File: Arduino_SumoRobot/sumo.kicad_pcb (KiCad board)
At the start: 2 copper layers, 66 x 53.3 mm, 45 parts, among them IC1 40106D, J1 HEADER_4, K1 RELAY_C, K2 RELAY_C, K3 RELAY_C, K4 RELAY_C, P1 Power, P10 CONN_01X04, P11 CONN_01X04, P12 CONN_01X02, P2 Analog, P3 Digital, P4 Digital, P5 CONN_1, P7 CONN_1, P9 CONN_01X06, Q1 S8050, Q2 S8050, Q3 S8050, Q4 S8050, U1 CNY70, U2 CNY70, U3 CNY70, U4 CNY70

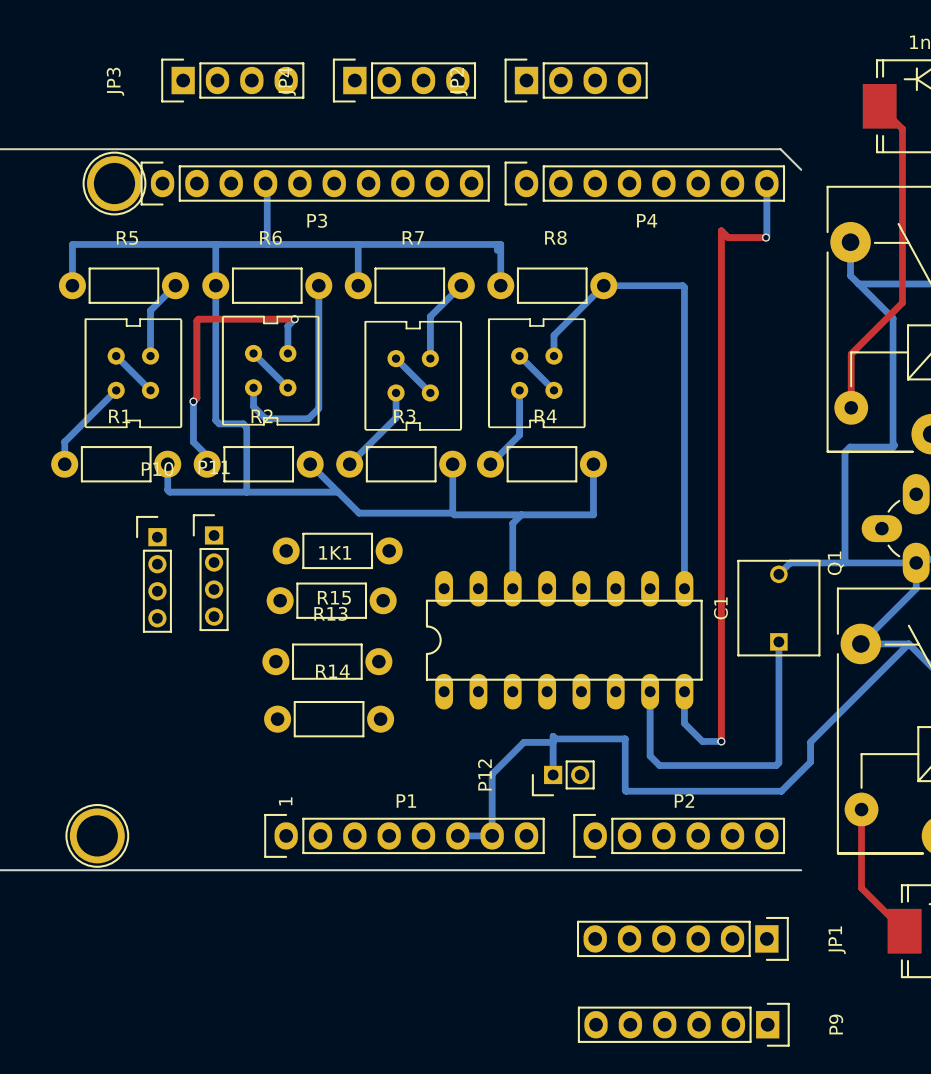
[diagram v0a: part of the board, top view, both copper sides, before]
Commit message: Reorganizo bibliotecas del Arduino_SumoRobot.
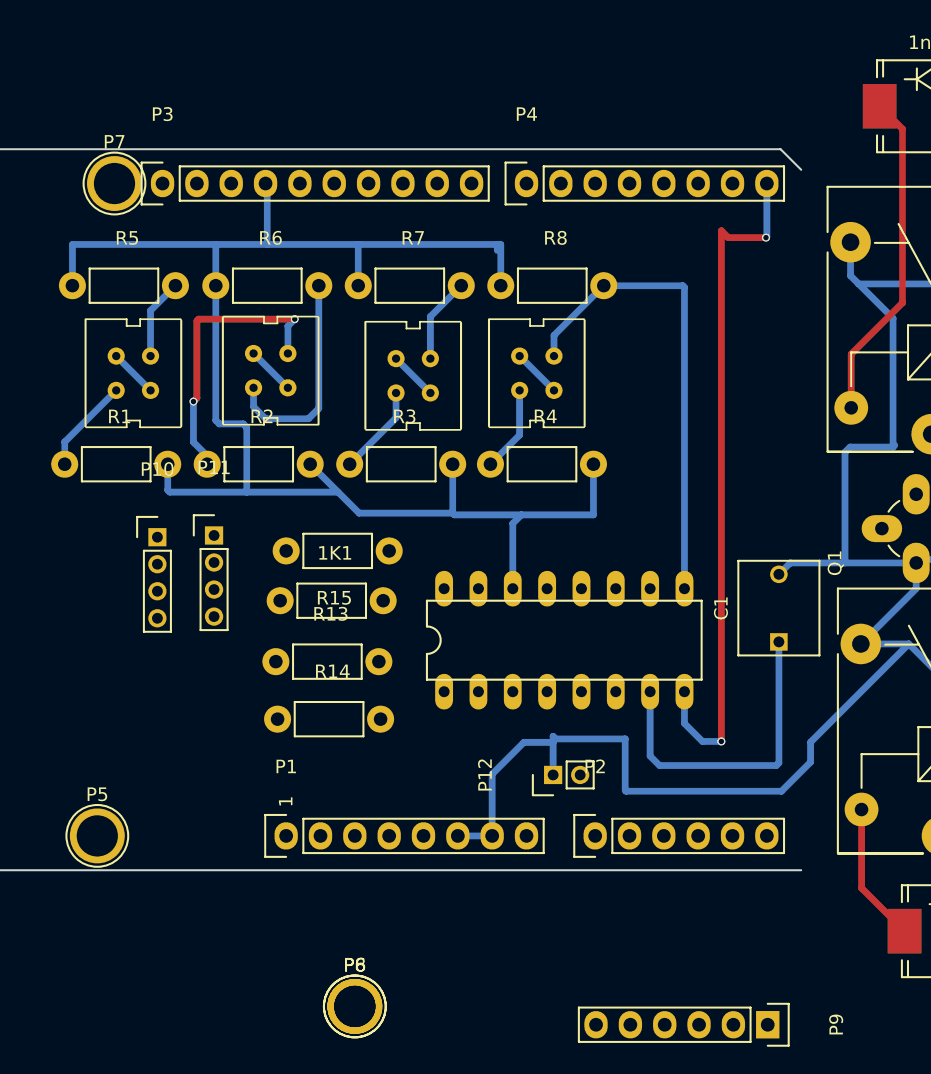
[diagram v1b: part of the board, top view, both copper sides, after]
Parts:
- removed JP1: PINHD-1X6, Pin_Headers:Pin_Header_Straight_1x06
- removed JP2, JP3, JP4: PINHD-1X4, Pin_Headers:Pin_Header_Straight_1x04
- added P6, P8: CONN_1, huellas:Arduino_1pin, F.Cu at (144.0, 136.4)
- 1K1, R1, R13, R14, R15, R2, R3, R4, R5, R6, R7, R8: footprint Resistors_ThroughHole:Resistor_Horizontal_RM7mm -> huellas:Resistor_Horizontal_RM7mm
- 1n1, 1n2, 1n3, 1n4: footprint Diodes_SMD:SMC_Standard -> huellas:SMC_Standard
- C1: footprint Capacitors_ThroughHole:C_Rect_L7_W6_P5 -> huellas:C_Rect_L7_W6_P5
- IC1: footprint 40xx:40xx-DIL16 -> huellas:40xx-DIL16
- J1: footprint Pin_Headers:Pin_Header_Straight_1x04 -> huellas:Pin_Header_Straight_1x04
- K1, K2, K3, K4: footprint Relays_ThroughHole:Relay_SANYOU_SRD_Series_Form_C -> huellas:Relay_SANYOU_SRD_Series_Form_C
- P1, P4: footprint Socket_Arduino_Uno:Socket_Strip_Arduino_1x08 -> huellas:Socket_Strip_Arduino_1x08
- P10, P11: footprint Pin_Headers:Pin_Header_Straight_1x04_Pitch2.00mm -> huellas:Pin_Header_Straight_1x04_Pitch2.00mm
- P12: footprint Pin_Headers:Pin_Header_Straight_1x02_Pitch2.00mm -> huellas:Pin_Header_Straight_1x02_Pitch2.00mm
- P2: footprint Socket_Arduino_Uno:Socket_Strip_Arduino_1x06 -> huellas:Socket_Strip_Arduino_1x06
- P3: footprint Socket_Arduino_Uno:Socket_Strip_Arduino_1x10 -> huellas:Socket_Strip_Arduino_1x10
- P5, P7: footprint Socket_Arduino_Uno:Arduino_1pin -> huellas:Arduino_1pin
- P9: footprint Pin_Headers:Pin_Header_Straight_1x06 -> huellas:Pin_Header_Straight_1x06
- Q1, Q2, Q3, Q4: footprint TO_SOT_Packages_THT:TO-92_Rugged -> huellas:TO-92_Rugged
- U1, U2, U3, U4: footprint cny70:cny70-4 -> huellas:cny70-4
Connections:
- K1 pad 3: +12V -> (no net)
- K2 pad 3: +12V -> (no net)
- K3 pad 3: +12V -> (no net)
- K4 pad 3: +12V -> (no net)
- P1 pad 1: Net-(P1-Pad1) -> (no net)
- P1 pad 2: /IOREF -> (no net)
- P1 pad 3: /Reset -> (no net)
- P1 pad 4: Net-(P1-Pad4) -> (no net)
- P1 pad 5: Net-(P1-Pad5) -> (no net)
- P1 pad 8: Net-(P1-Pad8) -> (no net)
- P10 pad 4: Net-(P10-Pad4) -> (no net)
- P11 pad 4: Net-(P11-Pad4) -> (no net)
- P12 pad 2: +12V -> (no net)
- P3 pad 1: Net-(P3-Pad1) -> (no net)
- P3 pad 2: Net-(P3-Pad2) -> (no net)
- P3 pad 3: Net-(P3-Pad3) -> (no net)
- P3 pad 5: Net-(P3-Pad5) -> (no net)
- P3 pad 6: Net-(P3-Pad6) -> (no net)
- P5 pad 1: Net-(P5-Pad1) -> (no net)
- P7 pad 1: Net-(P7-Pad1) -> (no net)
- U1 pad A: /VCC -> (no net)
- U1 pad C: /VCC -> (no net)
- U2 pad A: Net-(U2-PadA) -> (no net)
- U2 pad C: Net-(U2-PadA) -> (no net)
- U3 pad A: Net-(U3-PadA) -> (no net)
- U3 pad C: Net-(U3-PadA) -> (no net)
- U4 pad A: Net-(U4-PadA) -> (no net)
- U4 pad C: Net-(U4-PadA) -> (no net)
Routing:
- net (no net): track 0.00 -> 59.1 mm
- net +12V: track 44.7 -> 0.00 mm
- net /VCC: track 3.59 -> 0.00 mm
- net Net-(U4-PadA): track 3.59 -> 0.00 mm
- net Net-(U3-PadA): track 3.59 -> 0.00 mm
- net Net-(U2-PadA): track 3.59 -> 0.00 mm

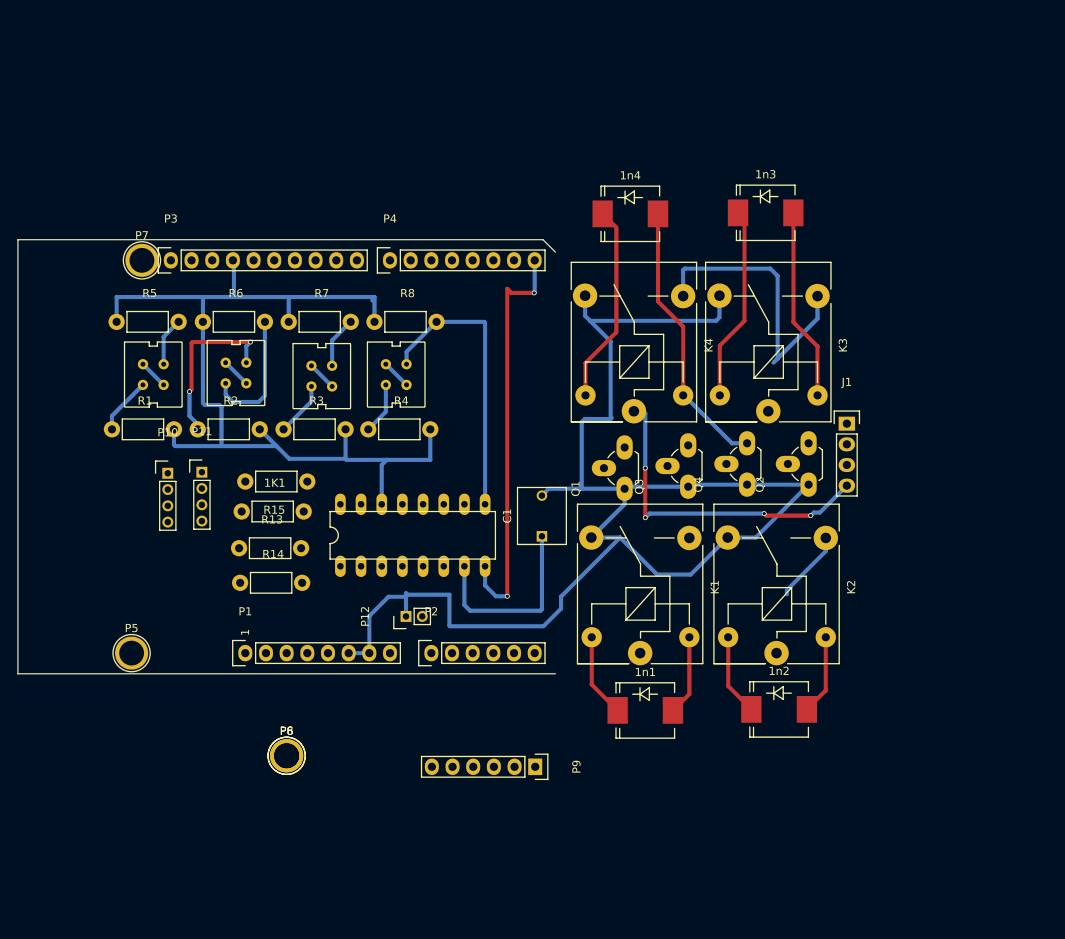
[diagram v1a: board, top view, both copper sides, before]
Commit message: Agrego avances y algunas correcciones propias: etiquetas 5V, serigrafía, prolijidad.
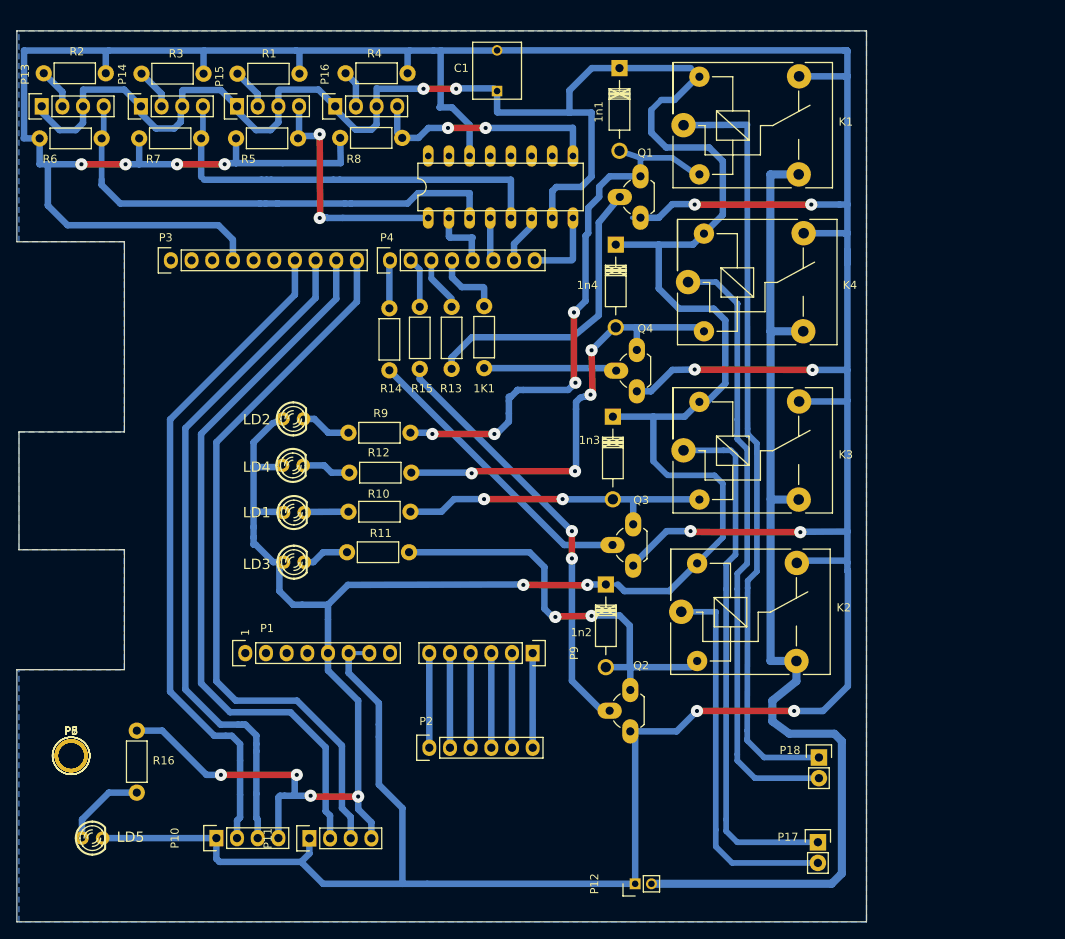
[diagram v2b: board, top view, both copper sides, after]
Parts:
- removed J1: HEADER_4, huellas:Pin_Header_Straight_1x04
- removed U1, U2, U3, U4: CNY70, huellas:cny70-4
- added LD1: LED3MM, Led:led-LED3MM, F.Cu at (144.9, 106.6)
- added LD2: LED3MM, Led:led-LED3MM, F.Cu at (144.8, 95.0)
- added LD3: LED3MM, Led:led-LED3MM, F.Cu at (144.9, 112.6)
- added LD4: LED3MM, Led:led-LED3MM, F.Cu at (144.8, 100.8)
- added LD5: LED3MM, Led:led-LED3MM, F.Cu at (120.1, 146.6)
- added P13: CONN_01X04, Pin_Headers:Pin_Header_Straight_1x04, F.Cu at (113.9, 56.6)
- added P14: CONN_01X04, Pin_Headers:Pin_Header_Straight_1x04, F.Cu at (126.1, 56.6)
- added P15: CONN_01X04, Pin_Headers:Pin_Header_Straight_1x04, F.Cu at (137.9, 56.6)
- added P16: CONN_01X04, Pin_Headers:Pin_Header_Straight_1x04, F.Cu at (150.0, 56.6)
- added P17: CONN_01X02, Pin_Headers:Pin_Header_Straight_1x02, F.Cu at (209.3, 147.1)
- added P18: CONN_01X02, Pin_Headers:Pin_Header_Straight_1x02, F.Cu at (209.4, 136.7)
- added R10: 220, huellas:Resistor_Horizontal_RM7mm, F.Cu at (151.6, 106.5)
- added R11: 220, huellas:Resistor_Horizontal_RM7mm, F.Cu at (151.4, 111.4)
- added R12: 220, huellas:Resistor_Horizontal_RM7mm, F.Cu at (151.7, 101.7)
- added R16: 220, huellas:Resistor_Horizontal_RM7mm, F.Cu at (125.6, 133.3)
- added R9: 220, huellas:Resistor_Horizontal_RM7mm, F.Cu at (151.6, 96.7)
- 1n1, 1n2, 1n3, 1n4: footprint huellas:SMC_Standard -> Diodes_ThroughHole:Diode_DO-41_SOD81_Horizontal_RM10
- P10, P11: footprint huellas:Pin_Header_Straight_1x04_Pitch2.00mm -> huellas:Pin_Header_Straight_1x04
- moved 1n1 79.0 mm to (184.9, 51.9), turned to 270 degrees
- moved K1 65.1 mm to (192.8, 59.0), turned to 0 degrees
- moved P7 61.5 mm to (117.5, 136.4)
- moved C1 55.0 mm to (169.9, 54.8)
- moved R2 47.7 mm to (114.2, 52.6)
- moved R3 47.1 mm to (126.2, 52.6)
- moved P11 46.9 mm to (146.8, 146.6), turned to 90 degrees
- moved R1 46.3 mm to (138.0, 52.6)
- moved P10 45.2 mm to (135.4, 146.6), turned to 90 degrees
- moved IC1 44.1 mm to (170.3, 66.5)
- moved R4 43.8 mm to (151.3, 52.6)
- moved P12 43.3 mm to (186.8, 152.2)
- moved Q2 37.4 mm to (186.2, 133.4)
- moved 1K1 34.6 mm to (168.3, 88.8), turned to 90 degrees
- moved R13 34.2 mm to (164.3, 88.9), turned to 90 degrees
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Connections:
- 1n1 pad 1: Net-(1n1-Pad1) -> +5V
- 1n2 pad 1: Net-(1n2-Pad1) -> +5V
- 1n3 pad 1: Net-(1n3-Pad1) -> +5V
- 1n4 pad 1: Net-(1n4-Pad1) -> +5V
- C1 pad 1: Net-(C1-Pad1) -> +5V
- IC1 pad 7: Net-(C1-Pad1) -> +5V
- K1 pad 5: Net-(1n1-Pad1) -> +5V
- K2 pad 5: Net-(1n2-Pad1) -> +5V
- K3 pad 5: Net-(1n3-Pad1) -> +5V
- K4 pad 5: Net-(1n4-Pad1) -> +5V
- P1 pad 5: (no net) -> +5V
- P10 pad 4: (no net) -> +5V
- P11 pad 4: (no net) -> +5V
- R13 pad 1: Net-(Q3-Pad2) -> Net-(Q1-Pad2)
- R14 pad 1: Net-(Q1-Pad2) -> Net-(Q3-Pad2)
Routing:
- net +5V: track 0.00 -> 398.6 mm, vias 0 -> 8
- net GND: track 289.1 -> 568.6 mm, vias 0 -> 12
- net Net-(K1-Pad1): track 0.00 -> 94.2 mm
- net /8: track 0.00 -> 89.4 mm
- net /9(**): track 0.00 -> 88.8 mm
- net /10(**/SS): track 0.00 -> 83.1 mm
- net /11(**/MOSI): track 0.00 -> 82.3 mm
- net (no net): track 59.1 -> 132.5 mm
- net Net-(K3-Pad1): track 0.00 -> 65.2 mm
- net Net-(1n1-Pad2): track 9.83 -> 69.1 mm, vias 0 -> 4
- net Net-(Q2-Pad2): track 0.00 -> 52.2 mm, vias 0 -> 2
- net Net-(K2-Pad1): track 0.00 -> 46.5 mm
- net Net-(IC1-Pad5): track 6.34 -> 51.7 mm
- net Net-(1n2-Pad2): track 9.84 -> 53.7 mm, vias 0 -> 2
- net Net-(IC1-Pad3): track 16.0 -> 59.6 mm
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- added copper zone on B.Cu, net GND
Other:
- board size 66 x 53.3 mm -> 104.4 x 109.5 mm
- net class Default: clearance 0.6 -> 0.5
- rule trace_clearance: 0.6 -> 0.5

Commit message: Corrijo Dip16 a Dip14, Corrijo net 12V, Limpio placa para rerutear.
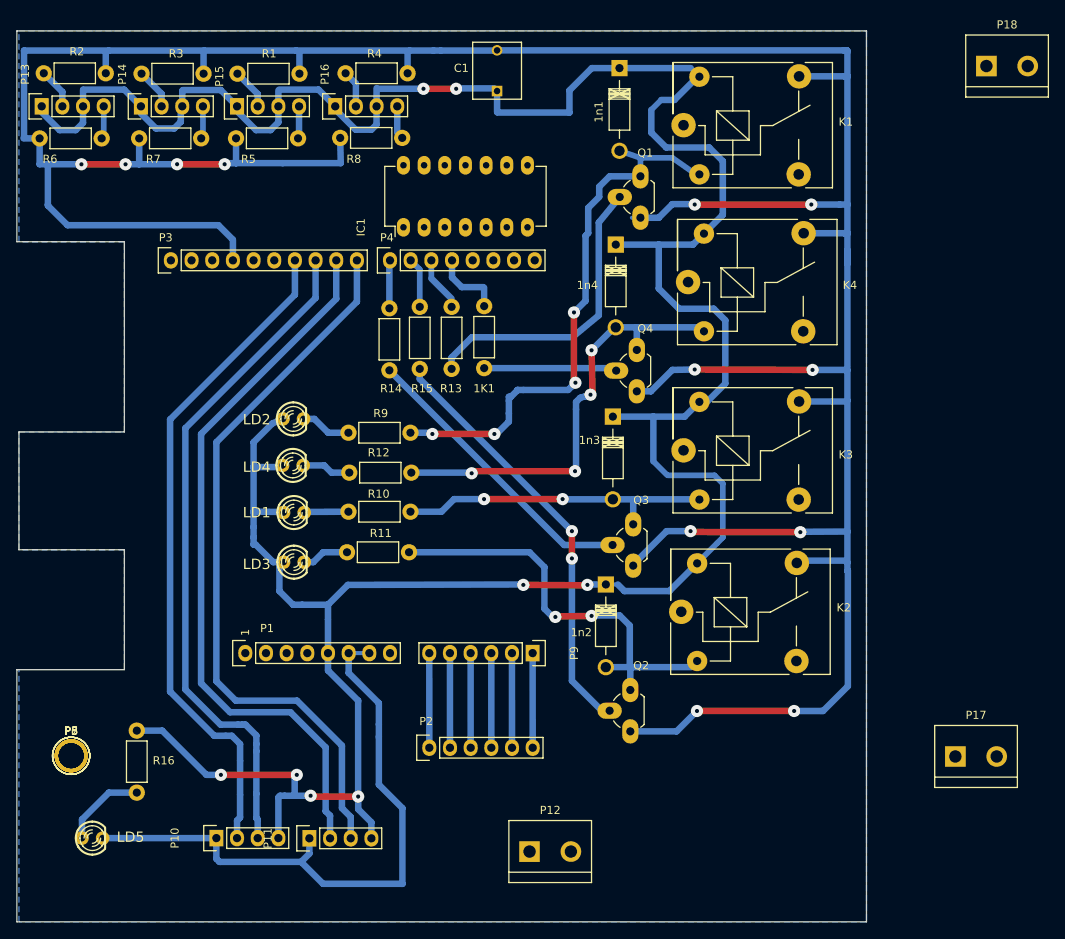
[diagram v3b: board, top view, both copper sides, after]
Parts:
- IC1: footprint huellas:40xx-DIL16 -> Housings_DIP:DIP-14_W7.62mm_LongPads
- P12: footprint huellas:Pin_Header_Straight_1x02_Pitch2.00mm -> Connect:bornier2
- P17, P18: footprint Pin_Headers:Pin_Header_Straight_1x02 -> Connect:bornier2
- moved P18 88.1 mm to (232.5, 51.7)
- moved P17 22.1 mm to (228.7, 136.5)
- moved IC1 12.9 mm to (158.4, 71.5), turned to 90 degrees
- moved P12 11.2 mm to (176.4, 148.2), turned to 0 degrees
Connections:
- IC1 pad 14: GND -> +5V
- IC1 pad 7: +5V -> GND
- K1 pad 3: (no net) -> +12V
- K2 pad 3: (no net) -> +12V
- K3 pad 3: (no net) -> +12V
- K4 pad 3: (no net) -> +12V
- P12 pad 2: (no net) -> +12V
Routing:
- net (no net): track 132.5 -> 0.00 mm
- net Net-(K1-Pad1): track 94.2 -> 0.00 mm
- net Net-(K4-Pad1): track 75.3 -> 0.00 mm
- net Net-(K3-Pad1): track 65.2 -> 0.00 mm
- net GND: track 568.6 -> 506.4 mm
- net Net-(IC1-Pad3): track 59.6 -> 4.04 mm
- net Net-(IC1-Pad5): track 51.7 -> 4.02 mm
- net Net-(K2-Pad1): track 46.5 -> 0.00 mm
- net Net-(IC1-Pad1): track 31.0 -> 4.28 mm, vias 2 -> 0
- net Net-(IC1-Pad9): track 29.1 -> 4.13 mm, vias 2 -> 0
- net +5V: track 398.6 -> 379.1 mm
- net /0(Rx): track 10.2 -> 0.36 mm
- net /3(**): track 8.20 -> 0.00 mm
- net /1(Tx): track 6.10 -> 0.00 mm
- net /2: track 5.36 -> 0.54 mm

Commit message: Correcciones varias, serigrafía, ruteo, borneras, puentes, planos, etc.
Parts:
- moved P5 97.8 mm to (176.7, 58.5)
- moved LD5 82.0 mm to (183.0, 93.9), turned to 90 degrees
- moved R16 79.1 mm to (194.2, 93.9), turned to 180 degrees
- moved P8 77.1 mm to (193.9, 146.7)
- moved P7 70.0 mm to (118.0, 66.4)
- moved LD2 58.6 mm to (186.1, 53.5), turned to 180 degrees
- moved R9 53.0 mm to (182.2, 53.5), turned to 270 degrees
- moved P18 50.5 mm to (207.6, 95.6), turned to 90 degrees
- moved LD4 49.9 mm to (186.1, 72.8), turned to 180 degrees
- moved LD3 43.5 mm to (186.3, 126.1), turned to 180 degrees
- moved R12 41.5 mm to (183.4, 74.8), turned to 270 degrees
- moved LD1 41.2 mm to (186.1, 105.8), turned to 180 degrees
- moved R11 34.4 mm to (182.5, 126.1), turned to 270 degrees
- moved R10 30.6 mm to (182.2, 105.8), turned to 270 degrees
- moved P17 24.9 mm to (207.6, 149.7), turned to 90 degrees
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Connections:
- P17 pad 1: Net-(K3-Pad1) -> Net-(K2-Pad1)
- P17 pad 2: Net-(K2-Pad1) -> Net-(K3-Pad1)
- P18 pad 1: Net-(K1-Pad1) -> Net-(K4-Pad1)
- P18 pad 2: Net-(K4-Pad1) -> Net-(K1-Pad1)
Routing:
- net +12V: track 0.01 -> 146.9 mm
- net GND: track 506.4 -> 408.6 mm, vias 12 -> 8
- net Net-(1n1-Pad2): track 69.1 -> 15.2 mm, vias 4 -> 0
- net Net-(IC1-Pad3): track 4.04 -> 54.2 mm, vias 0 -> 2
- net Net-(K3-Pad1): track 0.00 -> 45.9 mm
- net Net-(K1-Pad1): track 0.00 -> 43.7 mm
- net Net-(IC1-Pad5): track 4.02 -> 47.7 mm, vias 0 -> 2
- net Net-(1n4-Pad2): track 54.7 -> 12.7 mm, vias 4 -> 0
- net Net-(1n2-Pad2): track 53.7 -> 14.2 mm, vias 2 -> 0
- net /6(**): track 6.18 -> 36.5 mm
- net Net-(K4-Pad1): track 0.00 -> 29.7 mm
- net Net-(K2-Pad1): track 0.00 -> 28.5 mm
- net Net-(1n3-Pad2): track 39.5 -> 14.3 mm, vias 2 -> 0
- net Net-(IC1-Pad1): track 4.28 -> 28.5 mm, vias 0 -> 2
- net /7: track 5.92 -> 29.8 mm
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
